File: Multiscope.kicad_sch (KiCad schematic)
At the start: 47 parts, among them J2 USB_B_Micro, SW1 SW_Push, SW3 SW_Push, U1 STM32F405RGTx, U10 INA233, U2 TSR_1-2433, U3 LT6202CS5, U4 LT6202CS5, U5 LT6202CS5, U6 LT6202CS5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

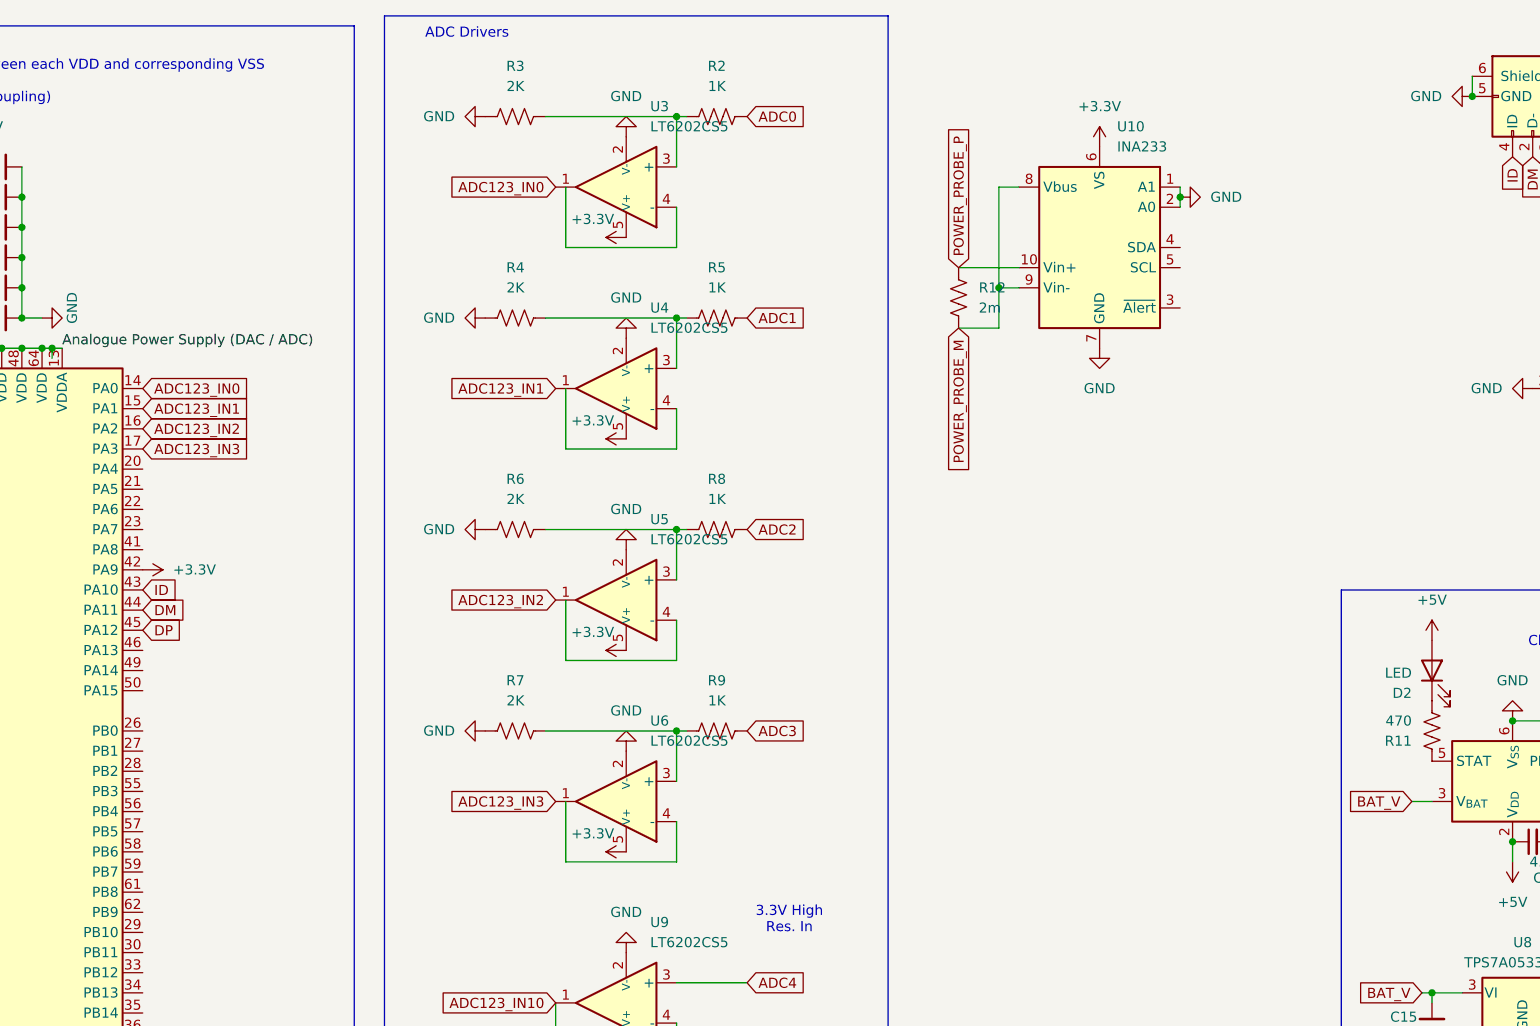
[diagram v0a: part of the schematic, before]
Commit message: setup i2c interface to metering ic
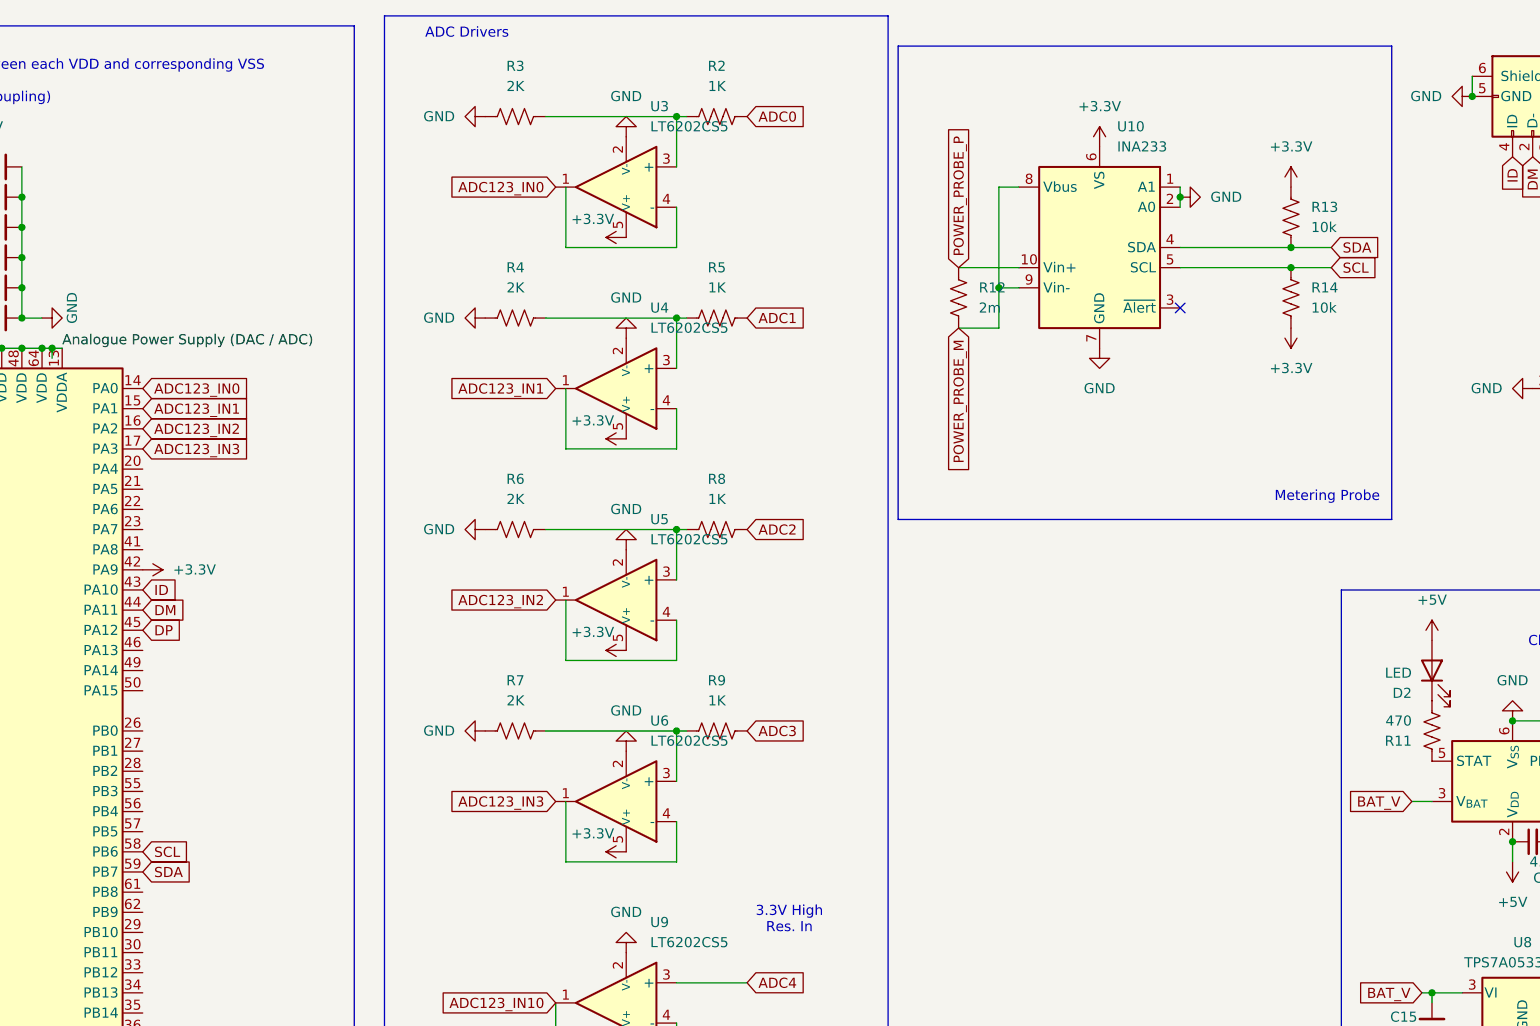
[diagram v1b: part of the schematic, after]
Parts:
- added R13, R14: 10k, symbol Device:R_US
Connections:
- net +3.3V: now also R13.1, R14.2
- net SCL: now reaches U1.58 (PB6)
- net SCL: now also U10.5 (SCL), R14.1
- net SDA: now reaches U1.59 (PB7)
- net SDA: now also U10.4 (SDA), R13.2
- no-connect marks 0 -> 1
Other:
- note added: "Metering Probe"
- company: (none) -> github.com/SuperliminalDefenestration
- title: (none) -> Multiscope Board 1

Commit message: added slave MCU, added proper power Auto-OR-ing (uses Schottkys), added variable v-supply input
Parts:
- removed D1: D_Schottky, symbol Device:D_Schottky
- added C18: 4.7uF, symbol Device:C_Small
- added F1, F2: Fuse_Small, symbol Device:Fuse_Small
- added R15: 100k, symbol Device:R_US
- added SW4: SW_SPST, symbol Switch:SW_SPST
- added U11: MCP4021-xxxxSN, Package_SO:SOIC-8_3.9x4.9mm_P1.27mm, symbol Potentiometer_Digital:MCP4021-xxxxSN
- added U12: LT6202CS5, PCM_Package_TO_SOT_SMD_AKL:SOT-23-5, symbol PCM_Amplifier_Operational_AKL:LT6202CS5
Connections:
- net +3.3V: now also U11.1 (VDD), U12.5 (V+)
- net +5V: now also SW4.2 (B)
- net ADC123_IN11: now also U12.1, U12.4 (-)
- net BAT_V: now also C18.2
- net GND: now also C18.1, R15.2, U11.2 (VSS), U12.2 (V-)
- net at D4.2 (A): now also F2.1; no longer U2.3 (Vout)
- net at C16.2, U8.2 (VO): now also F1.2; no longer D3.2 (A)
- net POT_UD: now reaches U1.26 (PB0)
- net POT_UD: now also U11.8 (U/~{D})
- net POT_CS: now reaches U1.27 (PB1)
- net POT_CS: now also U11.5 (~{CS})
- net VBUS: no longer names the net of J2.1 (VBUS)
- net VBUS: now also SW4.1 (A)
- new net: U11.4 (W), U12.3 (+)
- new net: R15.1, U11.6 (B)
- new net: D3.2 (A), F1.1
- new net: F2.2, U2.3 (Vout)
- new net ADC5: U11.3 (A)
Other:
- added sheet slaveMCU (slaveMCU.kicad_sch)
- note added: "Variable Voltage Input"
- moved on the sheet: D3, D4

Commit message: layout started
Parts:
- added J3, J4, J5, J6, J7, J8: Conn_01x01_Socket, Connector:Banana_Jack_1Pin, symbol Connector:Conn_01x01_Socket
- added R20, R21: 100k, PCM_Resistor_THT_AKL:R_Axial_DIN0204_L3.6mm_D1.6mm_P5.08mm_Horizontal, symbol Device:R
- added SW5, SW6: SW_Push, Button_Switch_THT:SW_PUSH_6mm, symbol Switch:SW_Push
- added SW7: SW_SPST, Button_Switch_THT:SW_SPST_Omron_B3F-40xx, symbol Switch:SW_SPST
- C1, C10, C11, C12, C13, C14, C15, C16, C18, C2, C3, C4, C5, C6, C7, C8, C9: footprint (none) -> Capacitor_THT:C_Axial_L3.8mm_D2.6mm_P7.50mm_Horizontal
- D2: footprint (none) -> LED_THT:LED_D8.0mm
- D3, D4: footprint (none) -> Diode_THT:D_DO-15_P10.16mm_Horizontal
- F1, F2: footprint (none) -> Fuse:Fuse_Blade_Mini_directSolder
- J2: footprint (none) -> Connector_USB:USB_Micro-AB_Molex_47590-0001
- R1, R10, R11, R12, R13, R14, R15, R2, R3, R4, R5, R6, R7, R8, R9: footprint (none) -> PCM_Resistor_THT_AKL:R_Axial_DIN0204_L3.6mm_D1.6mm_P5.08mm_Horizontal
- SW1, SW3: footprint (none) -> Button_Switch_THT:SW_PUSH_6mm
- SW4: footprint (none) -> Button_Switch_THT:SW_SPST_Omron_B3F-40xx
- Y1, Y2: footprint (none) -> Crystal:Crystal_DS10_D1.0mm_L4.3mm_Vertical
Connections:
- net +3.3V: now also SW5.2, SW6.2, SW7.2 (B); no longer D3.1 (K), D4.1 (K)
- net ADC0: now also J7.1 (Pin_1)
- net ADC1: now also J6.1 (Pin_1)
- net ADC2: now also J5.1 (Pin_1)
- net ADC3: now also J4.1 (Pin_1)
- net ADC4: now also J3.1 (Pin_1)
- net ADC5: now also J8.1 (Pin_1)
- net GND: now also R20.2, R21.2
- net SLAVE_SCK: now reaches U1.21 (PA5)
- net SLAVE_MISO: now reaches U1.22 (PA6)
- net SLAVE_MOSI: now reaches U1.23 (PA7)
- net at U1.35 (PB14): now also R21.1, SW6.1
- net at U1.36 (PB15): now also R20.1, SW5.1
- new net P_SWITCH: D3.1 (K), D4.1 (K), SW7.1 (A)

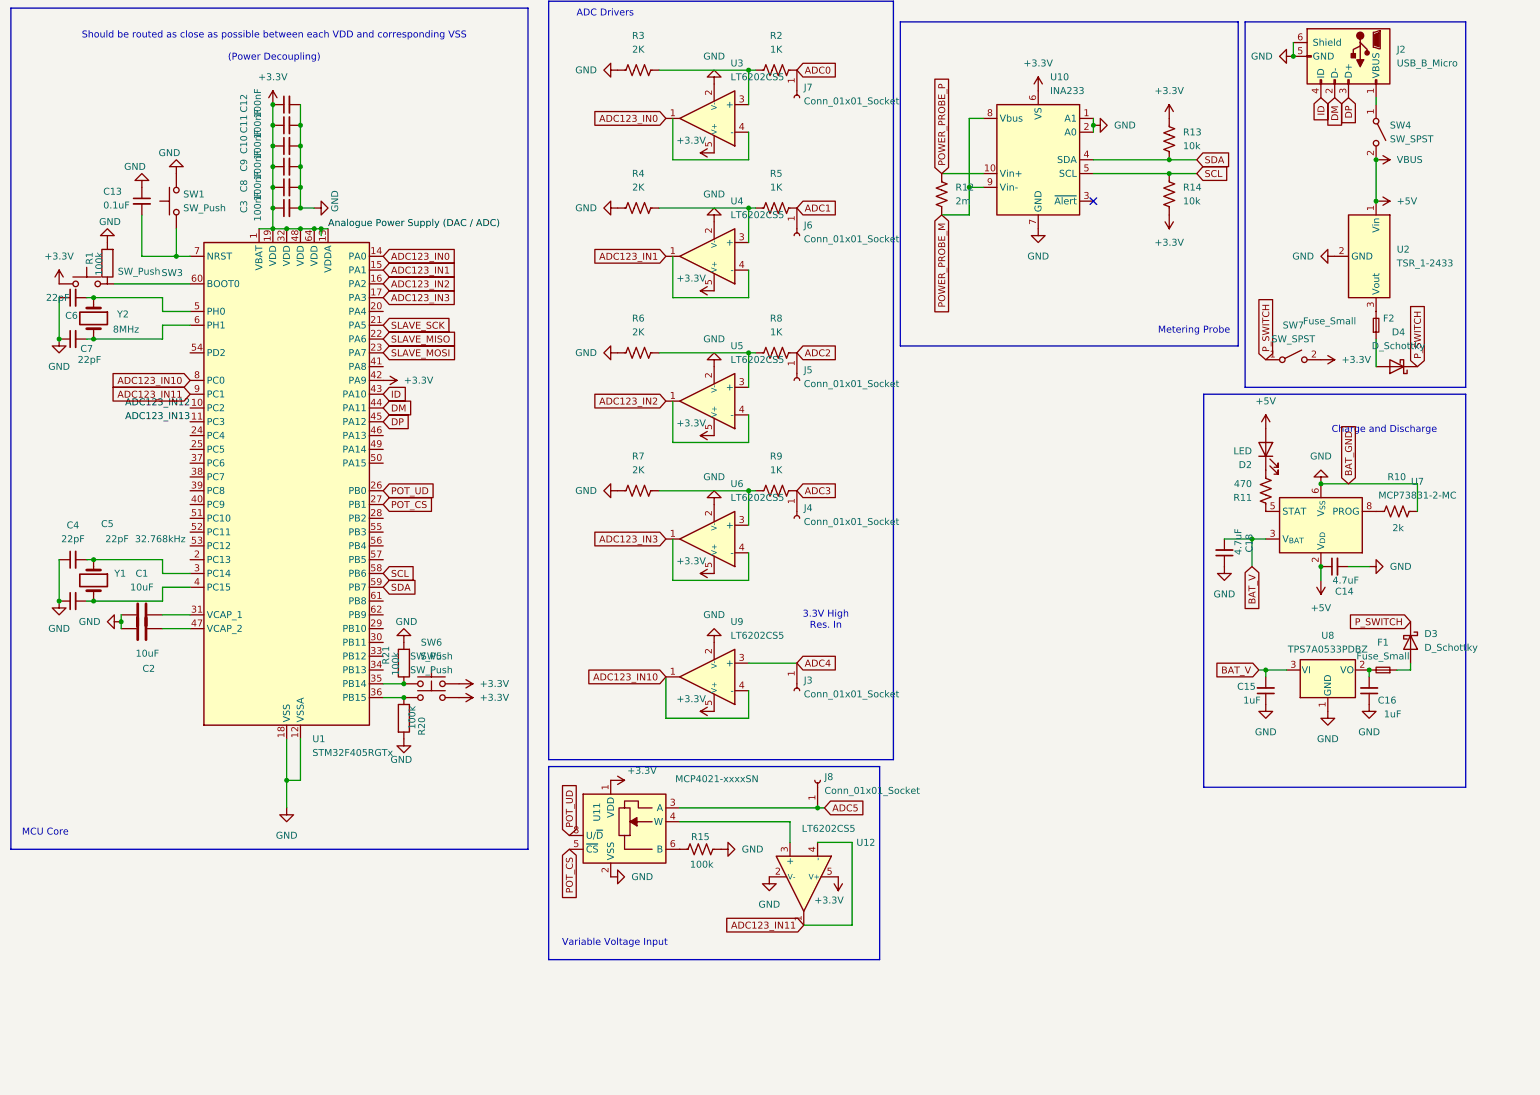
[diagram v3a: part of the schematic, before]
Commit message: Laid out traces for display
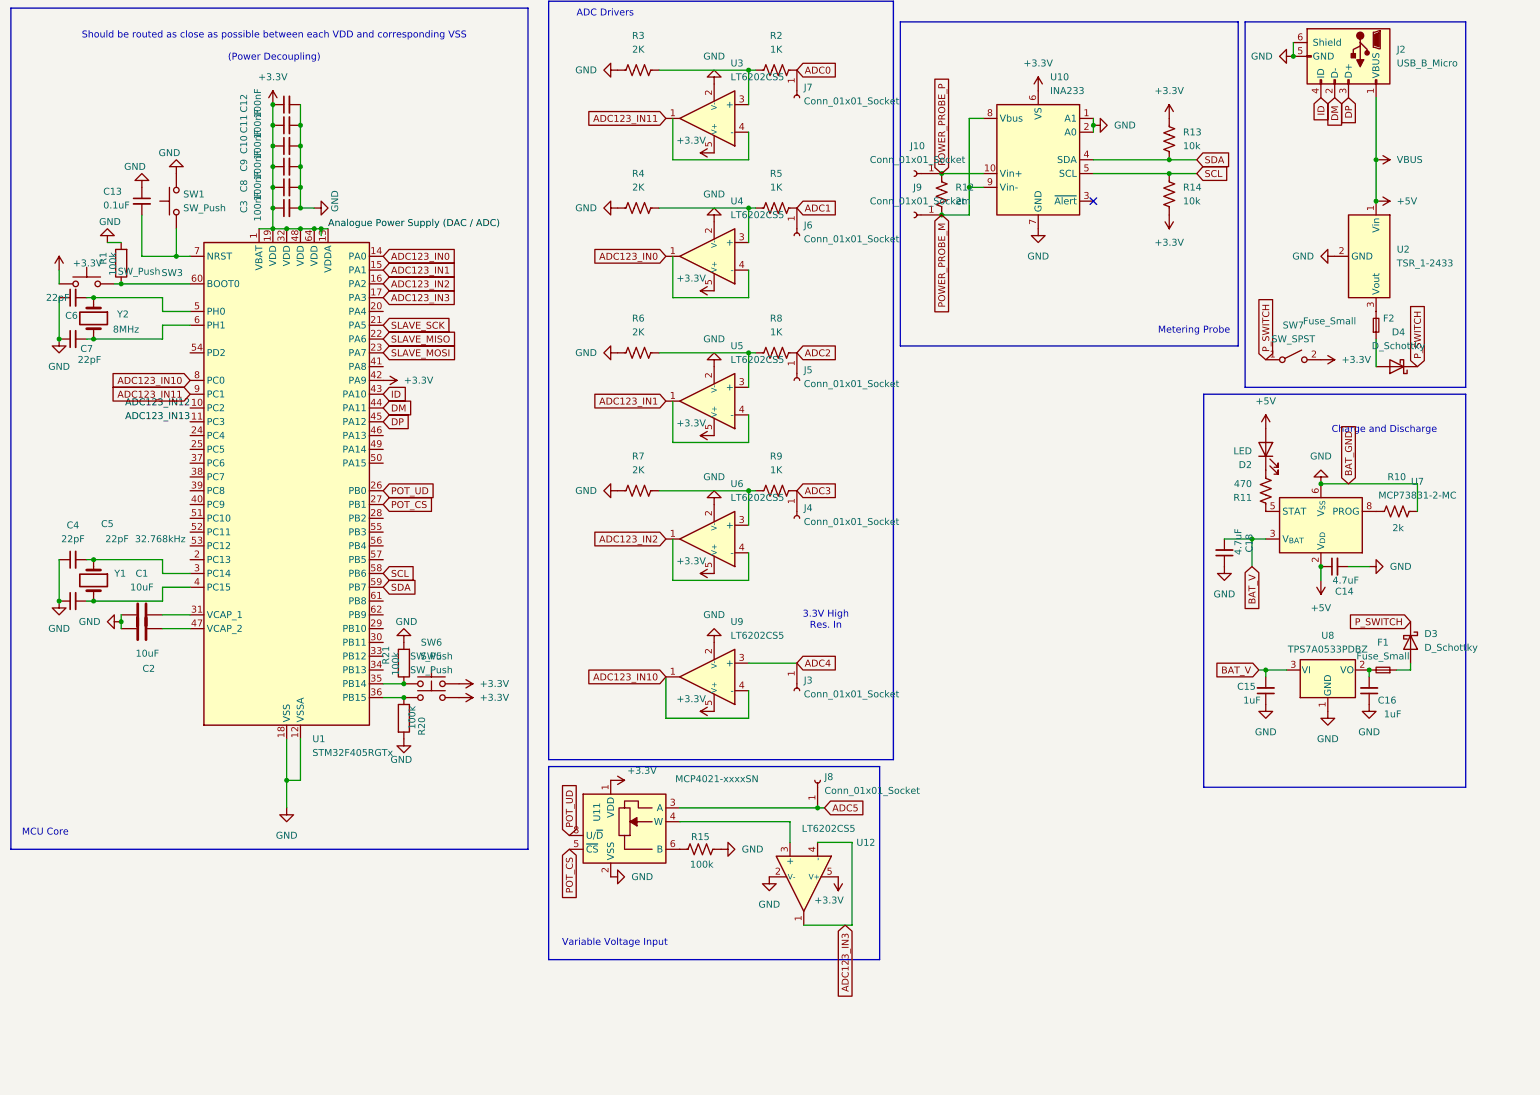
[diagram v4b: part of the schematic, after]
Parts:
- removed SW4: SW_SPST, Button_Switch_THT:SW_SPST_Omron_B3F-40xx, symbol Switch:SW_SPST
- added J10, J9: Conn_01x01_Socket, Connector:Banana_Jack_1Pin, symbol Connector:Conn_01x01_Socket
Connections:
- net +5V: now also J2.1 (VBUS)
- net ADC123_IN0: now also U4.1; no longer U3.1
- net ADC123_IN1: now also U5.1; no longer U4.1
- net ADC123_IN11: now also U3.1; no longer U12.1, U12.4 (-)
- net ADC123_IN2: now also U6.1; no longer U5.1
- net ADC123_IN3: now also U12.1, U12.4 (-); no longer U6.1
- net POWER_PROBE_M: now also J9.1 (Pin_1)
- net POWER_PROBE_P: now also J10.1 (Pin_1)
- net at R1.1: now also SW3.2, U1.60 (BOOT0)
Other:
- moved on the sheet: R1
